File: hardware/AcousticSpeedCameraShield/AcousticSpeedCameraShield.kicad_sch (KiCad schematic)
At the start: 0 parts

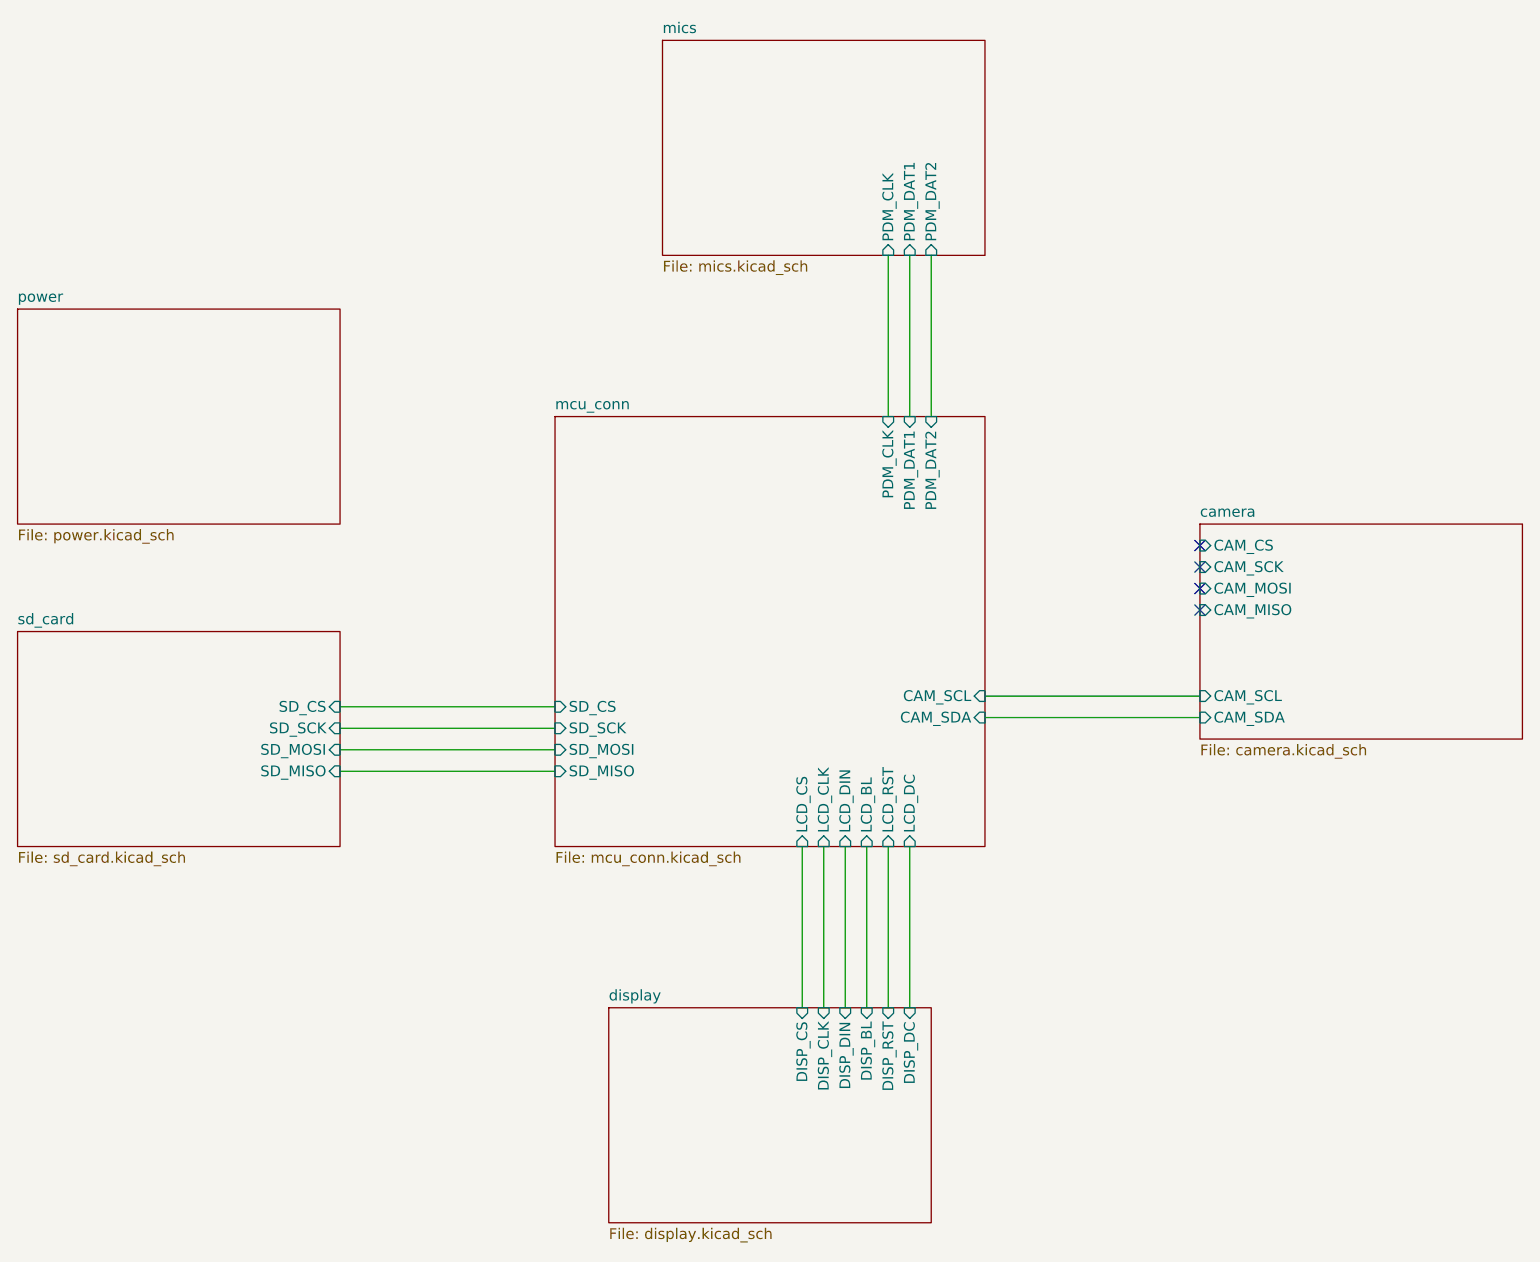
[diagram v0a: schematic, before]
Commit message: update MCU pin assignments
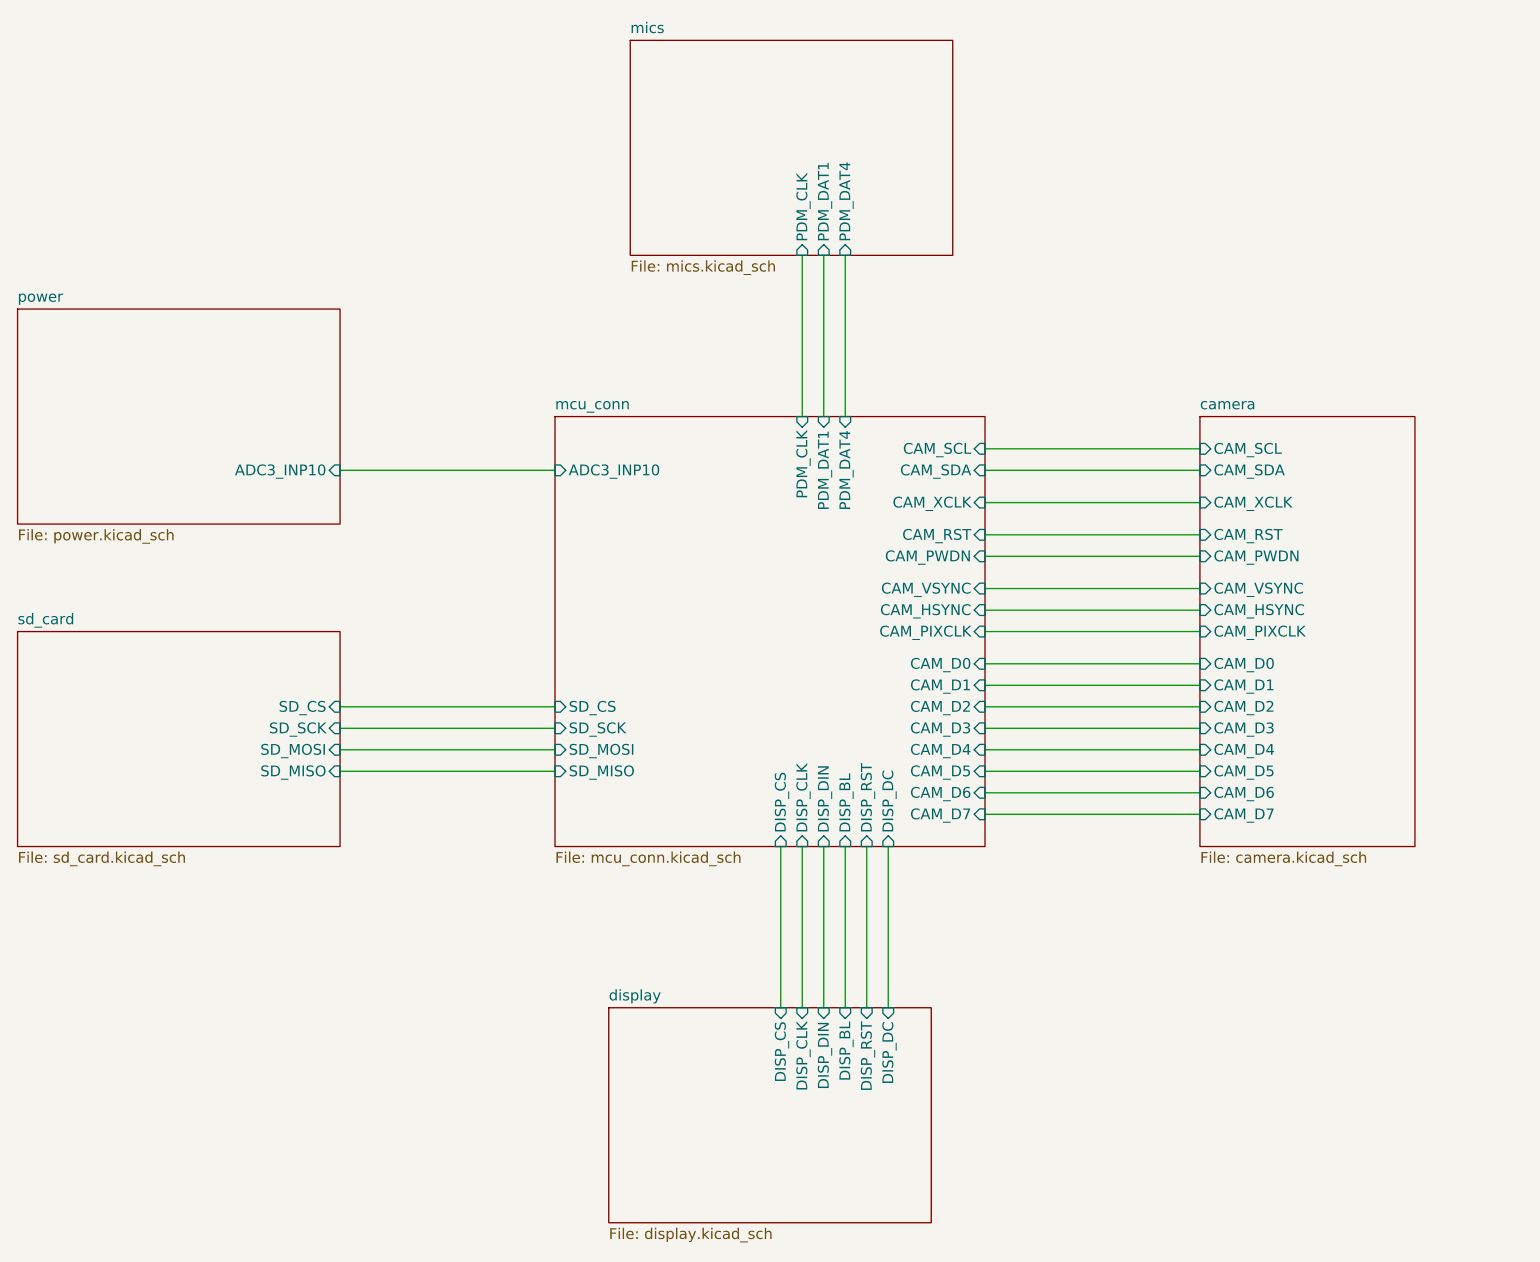
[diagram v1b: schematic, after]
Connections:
- no-connect marks 4 -> 0
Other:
- sheet camera ports: added CAM_D0, CAM_D1, CAM_D2, CAM_D3, CAM_D4, CAM_D5, CAM_D6, CAM_D7, CAM_HSYNC, CAM_PIXCLK, CAM_PWDN, CAM_RST, CAM_VSYNC, CAM_XCLK; removed CAM_CS, CAM_MISO, CAM_MOSI, CAM_SCK
- sheet mcu_conn ports: added ADC3_INP10, CAM_D0, CAM_D1, CAM_D2, CAM_D3, CAM_D4, CAM_D5, CAM_D6, CAM_D7, CAM_HSYNC, CAM_PIXCLK, CAM_PWDN, CAM_RST, CAM_VSYNC, CAM_XCLK, DISP_BL, DISP_CLK, DISP_CS, DISP_DC, DISP_DIN, DISP_RST, PDM_DAT4; removed LCD_BL, LCD_CLK, LCD_CS, LCD_DC, LCD_DIN, LCD_RST, PDM_DAT2
- sheet mics ports: added PDM_DAT4; removed PDM_DAT2
- sheet power ports: added ADC3_INP10; removed none
- title: (none) -> Nakładka STM32 - Schemat Ideowy
